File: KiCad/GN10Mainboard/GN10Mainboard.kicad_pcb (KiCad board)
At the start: 4 copper layers, 80 x 60 mm, 129 parts, among them J1 XT30PW-M, J10 USB_C_Receptacle_USB2.0, J13 Conn_01x06, J14 Conn_01x06, J4 Conn_01x04, J5 Conn_01x06, J6 Conn_01x04, J7 Conn_01x04, J8 Conn_01x04, J9 RJ45_Bel_SI-60062-F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

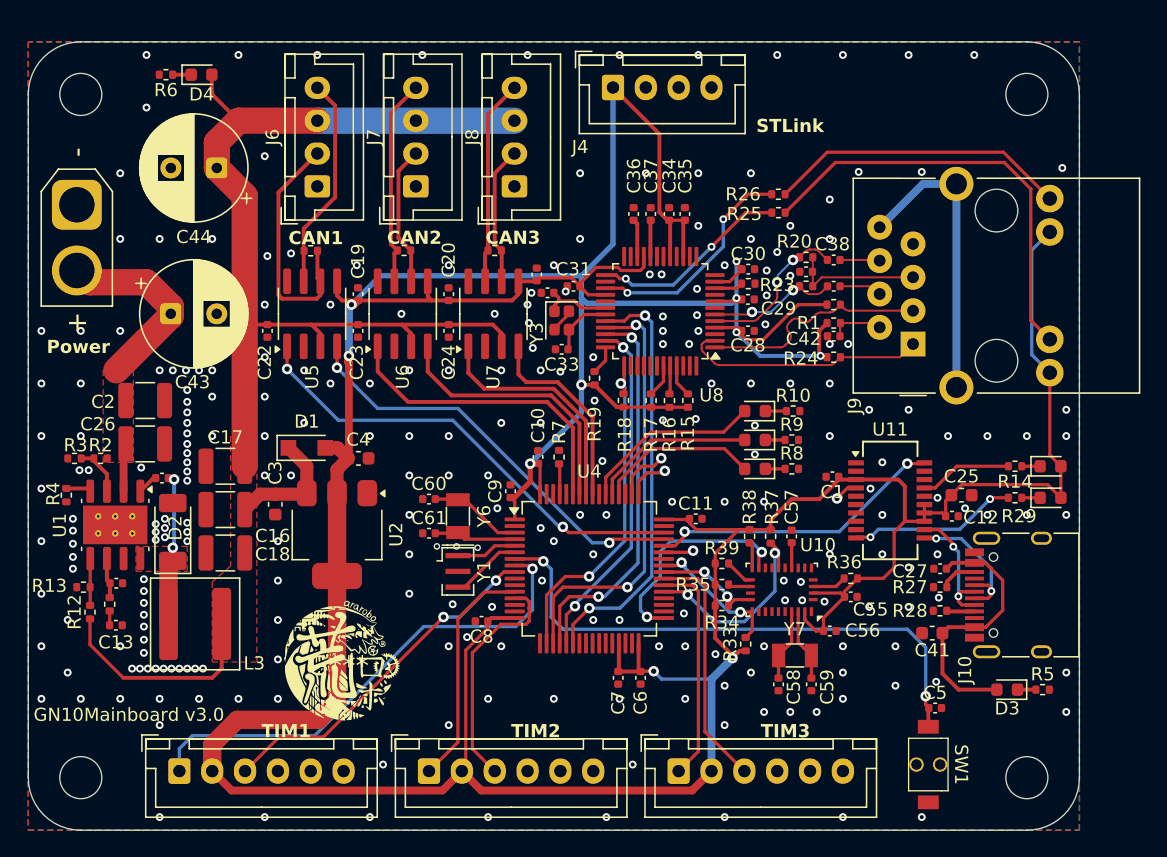
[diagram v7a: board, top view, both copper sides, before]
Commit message: remove:prev project, update:MCU to STM32H7
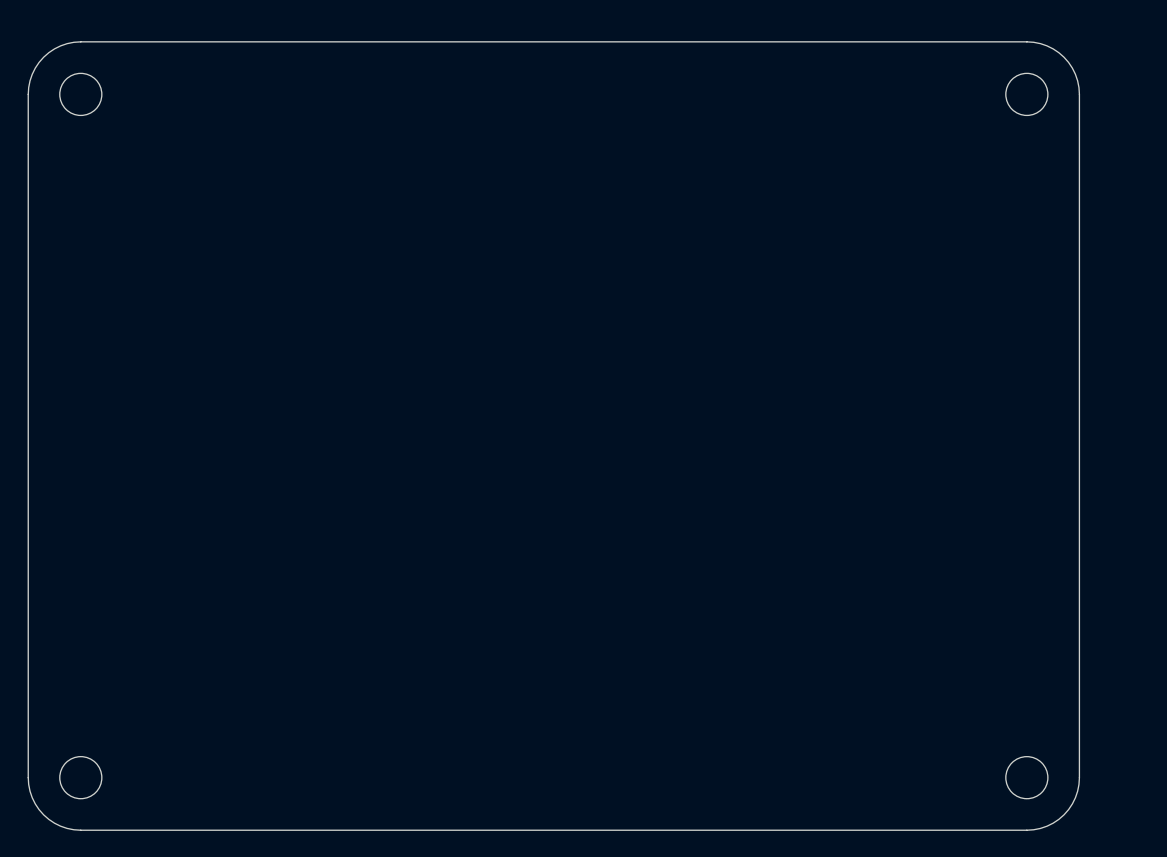
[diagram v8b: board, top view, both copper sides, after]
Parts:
- removed C1, C12, C15, C19, C20, C21, C22, C23, C24, C27, C29, C30, C31, C34, C5, C55, C56, C57, C6, C7, C8, C9: 0.1u, Capacitor_SMD:C_0402_1005Metric
- removed C10, C28: 1u, Capacitor_SMD:C_0402_1005Metric
- removed C11, C35, C37: 4.7u, Capacitor_SMD:C_0402_1005Metric
- removed C13: 4700p, Capacitor_SMD:C_0402_1005Metric
- removed C14: 47p, Capacitor_SMD:C_0402_1005Metric
- removed C16, C17, C18: 47u, Capacitor_SMD:C_1210_3225Metric
- removed C2, C26: 4.7u, Capacitor_SMD:C_1210_3225Metric
- removed C25, C41: 4.7u, Capacitor_SMD:C_0603_1608Metric
- removed C3, C4: 10u, Capacitor_SMD:C_0603_1608Metric
- removed C32, C33: 18p, Capacitor_SMD:C_0402_1005Metric
- removed C36, C39: 10n, Capacitor_SMD:C_0402_1005Metric
- removed C38, C40: 6.8n, Capacitor_SMD:C_0402_1005Metric
- removed C42: 22n, Capacitor_SMD:C_0402_1005Metric
- removed C43, C44: 100u, Capacitor_THT:CP_Radial_D8.0mm_P3.50mm
- removed C58, C59, C60, C61: 22p, Capacitor_SMD:C_0402_1005Metric
- removed D1: SS2040FL, Diode_SMD:Nexperia_CFP3_SOD-123W
- removed D2: RB088LAM-60TR, Diode_SMD:D_SOD-128
- removed D3, D4: White, LED_SMD:LED_0603_1608Metric
- removed D5: Red, LED_SMD:LED_0603_1608Metric
- removed D6: Green, LED_SMD:LED_0603_1608Metric
- removed D7: Blue, LED_SMD:LED_0603_1608Metric
- removed D8, D9: LED, LED_SMD:LED_0603_1608Metric
- removed G***: LOGO, GN10_Parts:ararobosmall
- removed J1: XT30PW-M, Connector_AMASS:AMASS_XT30U-M_1x02_P5.0mm_Vertical
- removed J10: USB_C_Receptacle_USB2.0, Connector_USB:USB_C_Receptacle_HRO_TYPE-C-31-M-12
- removed J13, J14, J5: Conn_01x06, Connector_JST:JST_XH_B6B-XH-A_1x06_P2.50mm_Vertical
- removed J4, J6, J7, J8: Conn_01x04, Connector_JST:JST_XH_B4B-XH-A_1x04_P2.50mm_Vertical
- removed J9: RJ45_Bel_SI-60062-F, Connector_RJ:RJ45_Bel_SI-60062-F
- removed L3: 6.8u, Inductor_SMD:L_Coilcraft_XAL6060-XXX
- removed R1: 10, Resistor_SMD:R_0402_1005Metric
- removed R10, R5, R6, R8, R9: 1k, Resistor_SMD:R_0402_1005Metric
- removed R11: 16.9k, Resistor_SMD:R_0402_1005Metric
- removed R12: 53.6k, Resistor_SMD:R_0402_1005Metric
- removed R13: 10.2k, Resistor_SMD:R_0402_1005Metric
- removed R14, R29: 470, Resistor_SMD:R_0402_1005Metric
- removed R15, R16, R17, R18, R19: PU, Resistor_SMD:R_0402_1005Metric
- removed R2: 442k, Resistor_SMD:R_0402_1005Metric
- removed R20, R21, R22, R24: 49, Resistor_SMD:R_0402_1005Metric
- removed R23: 12.4k, Resistor_SMD:R_0402_1005Metric
- removed R25, R26: R, Resistor_SMD:R_0402_1005Metric
- removed R27, R28: 4.7k, Resistor_SMD:R_0402_1005Metric
- removed R3: 90.9k, Resistor_SMD:R_0402_1005Metric
- removed R33, R34, R38, R39: 2.2k, Resistor_SMD:R_0402_1005Metric
- removed R35, R36, R37, R7: 10k, Resistor_SMD:R_0402_1005Metric
- removed R4: 243k, Resistor_SMD:R_0402_1005Metric
- removed R44, R45, R46: 120, Resistor_SMD:R_0402_1005Metric
- removed SW1: SW_Push, GN10_Parts:TVAF
- removed U1: TPS54560DDA, Package_SO:Texas_R-PDSO-G8_EP2.95x4.9mm_Mask2.4x3.1mm_ThermalVias
- removed U10: BNO086, Package_LGA:LGA-28_5.2x3.8mm_P0.5mm
- removed U11: FT231XS, Package_SO:SSOP-20_3.9x8.7mm_P0.635mm
- removed U2: 3.3V, Package_TO_SOT_SMD:SOT-223-3_TabPin2
- removed U4: STM32G474RETx, Package_QFP:LQFP-64_10x10mm_P0.5mm
- removed U5, U6, U7: MCP2562-E-SN, Package_SO:SOIC-8_3.9x4.9mm_P1.27mm
- removed U8: W5500, Package_QFP:LQFP-48_7x7mm_P0.5mm
- removed Y1: 24MHz, Crystal:Resonator_SMD_Murata_CSTxExxV-3Pin_3.0x1.1mm
- removed Y3: 25M, Crystal:Crystal_SMD_2016-4Pin_2.0x1.6mm
- removed Y6, Y7: 32.768kHz, Crystal:Crystal_SMD_3215-2Pin_3.2x1.5mm
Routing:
- net +3.3V: track 374.4 -> 0.00 mm, vias 10 -> 0
- net +5V: track 103.9 -> 0.00 mm
- net STM32_RESET: track 42.4 -> 0.00 mm, vias 2 -> 0
- net TIM1_CH1: track 37.5 -> 0.00 mm, vias 1 -> 0
- net CAN1_TX: track 35.6 -> 0.00 mm, vias 2 -> 0
- net SYS_SWDIO: track 34.0 -> 0.00 mm, vias 1 -> 0
- net SYS_SWCLK: track 33.7 -> 0.00 mm, vias 1 -> 0
- net Net-(J9-PadL2): track 33.1 -> 0.00 mm
- net SPI1_SCK: track 32.9 -> 0.00 mm, vias 2 -> 0
- net SPI1_CS: track 32.2 -> 0.00 mm, vias 2 -> 0
- net CAN1_RX: track 32.1 -> 0.00 mm, vias 2 -> 0
- net SPI1_MISO: track 29.6 -> 0.00 mm, vias 2 -> 0
- net TIM1_CH2: track 26.8 -> 0.00 mm, vias 2 -> 0
- net SPI1_MOSI: track 26.4 -> 0.00 mm, vias 2 -> 0
- net W5500_RST: track 25.8 -> 0.00 mm, vias 2 -> 0
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- removed copper zone on F.Cu, net +5V
- removed copper zone on F.Cu, net +BATT
- removed copper zone on B.Cu, net GND
- removed copper zone on F.Cu, net GND
- removed copper zone on In1.Cu, net GND
- removed copper zone on F.Cu, net Net-(D2-K)
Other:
- board text removed: "CAN1"
- board text removed: "CAN2"
- board text removed: "CAN3"
- board text removed: "GN10Mainboard v3.0"
- board text removed: "Power"
- board text removed: "STLink"
- board text removed: "TIM1"
- board text removed: "TIM2"
- board text removed: "TIM3"
- board text removed: "designed by aiba-gento"
